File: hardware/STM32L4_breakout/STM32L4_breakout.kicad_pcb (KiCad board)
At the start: 2 copper layers, 64 parts, among them J1 12V IN, J10 GPIO, J11 SPI1, J12 USART1, J13 USART3, J14 UART4, J15 3.3V, J16 5V, J17 12V, J2 SWD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

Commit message: breakout board PCB layout WIP
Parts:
- J2: footprint Connector_PinHeader_2.54mm:PinHeader_2x05_P2.54mm_Vertical -> Connector_PinHeader_2.54mm:PinHeader_1x06_P2.54mm_Vertical
- moved J2 109.7 mm to (145.5, 78.8), turned to 180 degrees
- moved C12 51.1 mm to (157.5, 69.5), turned to 90 degrees
- moved C11 51.0 mm to (157.5, 67.0), turned to -90 degrees
- moved X1 40.6 mm to (155.5, 68.2), turned to -90 degrees
- moved L1 39.5 mm to (158.2, 79.0)
- moved C21 34.7 mm to (159.5, 74.0), turned to 90 degrees
- moved C13 32.4 mm to (164.5, 79.2), turned to 180 degrees
- moved C20 31.9 mm to (158.5, 77.0), turned to 180 degrees
- moved C14 31.5 mm to (171.0, 79.2), turned to 180 degrees
- moved R18 29.3 mm to (159.2, 69.0)
- moved R16 27.4 mm to (159.2, 67.5)
- moved C16 22.8 mm to (175.8, 67.8), turned to -90 degrees
- moved C15 19.3 mm to (158.8, 71.5), turned to 180 degrees
- moved C18 6.47 mm to (164.2, 61.0)
- moved C19 5.41 mm to (177.8, 67.8), turned to 90 degrees
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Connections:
- J2 pad 3: GND -> SWCLK
- J2 pad 4: SWCLK -> SWO
- J2 pad 5: GND -> STM_NRST
- J2 pad 6: SWO -> GND

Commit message: breakout board PCB layout WIP
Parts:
- C11, C12: footprint Capacitor_SMD:C_0603_1608Metric -> Capacitor_SMD:C_0402_1005Metric
- R16, R18: footprint Resistor_SMD:R_0603_1608Metric -> Resistor_SMD:R_0402_1005Metric
- moved J1 96.3 mm to (129.9, 67.5), turned to -90 degrees
- moved J12 94.1 mm to (178.0, 47.5), turned to 90 degrees
- moved J9 89.6 mm to (149.5, 70.7)
- moved C2 89.5 mm to (161.2, 47.5), turned to -90 degrees
- moved C4 86.8 mm to (163.5, 47.2), turned to -90 degrees
- moved C6 83.9 mm to (168.8, 50.2)
- moved U2 81.5 mm to (166.8, 47.5)
- moved C3 80.7 mm to (142.8, 60.5), turned to 90 degrees
- moved C7 80.0 mm to (170.2, 47.5), turned to -90 degrees
- moved J8 77.4 mm to (169.2, 84.8), turned to 90 degrees
- moved C9 75.8 mm to (172.5, 47.2), turned to -90 degrees
- moved C1 74.6 mm to (128.8, 60.5), turned to 90 degrees
- moved J11 73.7 mm to (166.5, 89.5), turned to 90 degrees
- moved U1 72.9 mm to (135.8, 59.0), turned to 0 degrees
- moved C5 68.9 mm to (145.5, 60.5), turned to 90 degrees
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
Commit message: breakout board PCB layout WIP
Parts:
- C11, C12: footprint Capacitor_SMD:C_0402_1005Metric -> Capacitor_SMD:C_0603_1608Metric
- R16, R18: footprint Resistor_SMD:R_0402_1005Metric -> Resistor_SMD:R_0603_1608Metric
- moved J14 111.5 mm to (149.5, 78.0)
- moved J13 96.7 mm to (150.0, 93.8), turned to 90 degrees
- moved J10 24.1 mm to (197.8, 62.8)
- moved J8 12.6 mm to (178.0, 93.8)
- moved J7 4.75 mm to (187.5, 62.5)
- moved J11 4.52 mm to (165.0, 93.8)
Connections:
- J10 pad 2: TFT_CS -> RELAY2_CTRL
- J10 pad 3: CARDCS_5V -> TFT_DC
- J10 pad 4: D7 -> RT_CS
- J10 pad 5: TFT_DC -> RELAY1_CTRL
- J10 pad 7: RELAY1_CTRL -> D7
- J10 pad 8: RT_CS -> CARDCS_5V
- J10 pad 9: RELAY2_CTRL -> TFT_CS

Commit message: breakout board layout WIP
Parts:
- moved R15 52.1 mm to (123.3, 110.7), turned to -90 degrees
- moved R14 34.4 mm to (128.1, 146.7), turned to 90 degrees
- moved J3 31.4 mm to (128.1, 139.1), turned to 90 degrees
- moved R12 29.8 mm to (166.2, 145.5), turned to 90 degrees
- moved R11 26.9 mm to (163.7, 145.5), turned to 90 degrees
- moved J6 25.6 mm to (168.3, 114.8), turned to -90 degrees
- moved R10 24.0 mm to (161.1, 145.5), turned to 90 degrees
- moved J5 22.6 mm to (141.1, 116.3), turned to -90 degrees
- moved R9 21.4 mm to (158.6, 145.5), turned to 90 degrees
- moved R13 19.3 mm to (145.9, 149.3), turned to -90 degrees
- moved R8 19.2 mm to (156.0, 145.5), turned to 90 degrees
- moved R7 17.3 mm to (153.5, 145.5), turned to 90 degrees
- moved J4 6.19 mm to (153.5, 139.1), turned to 90 degrees
- moved R4 1.31 mm to (105.5, 127.0)
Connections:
- net Net-(J5-Pad8) renamed /ARD_3V3A
- net Net-(R1-Pad2) renamed /I2C_PULL_3V3

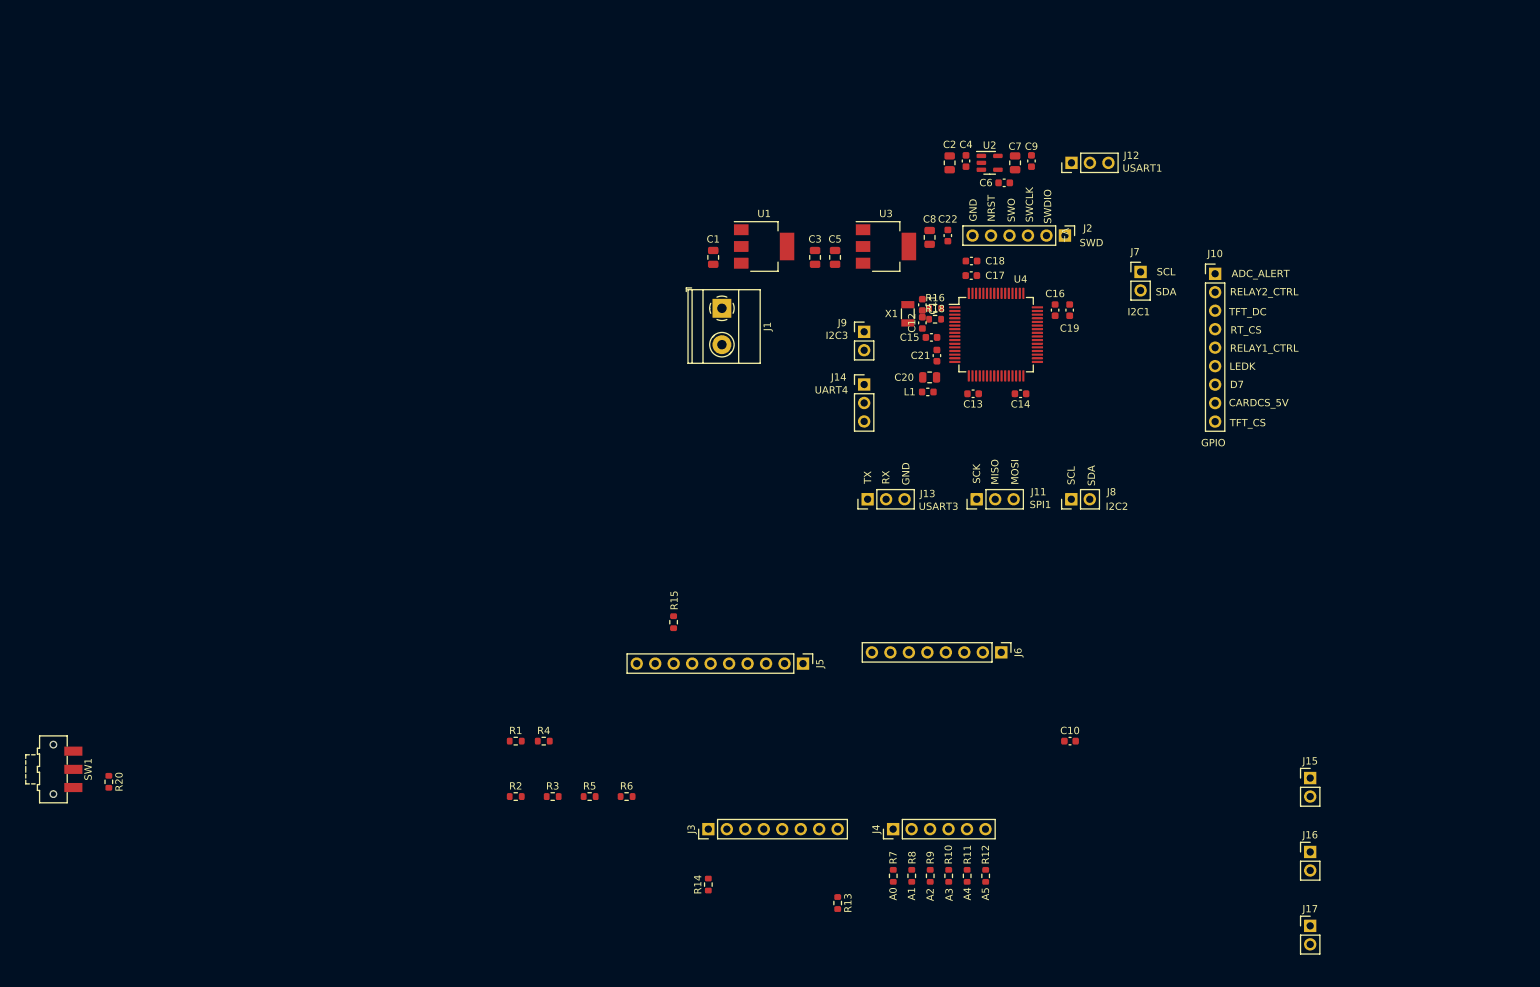
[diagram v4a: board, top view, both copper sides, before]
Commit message: breakout board pcb layout WIP
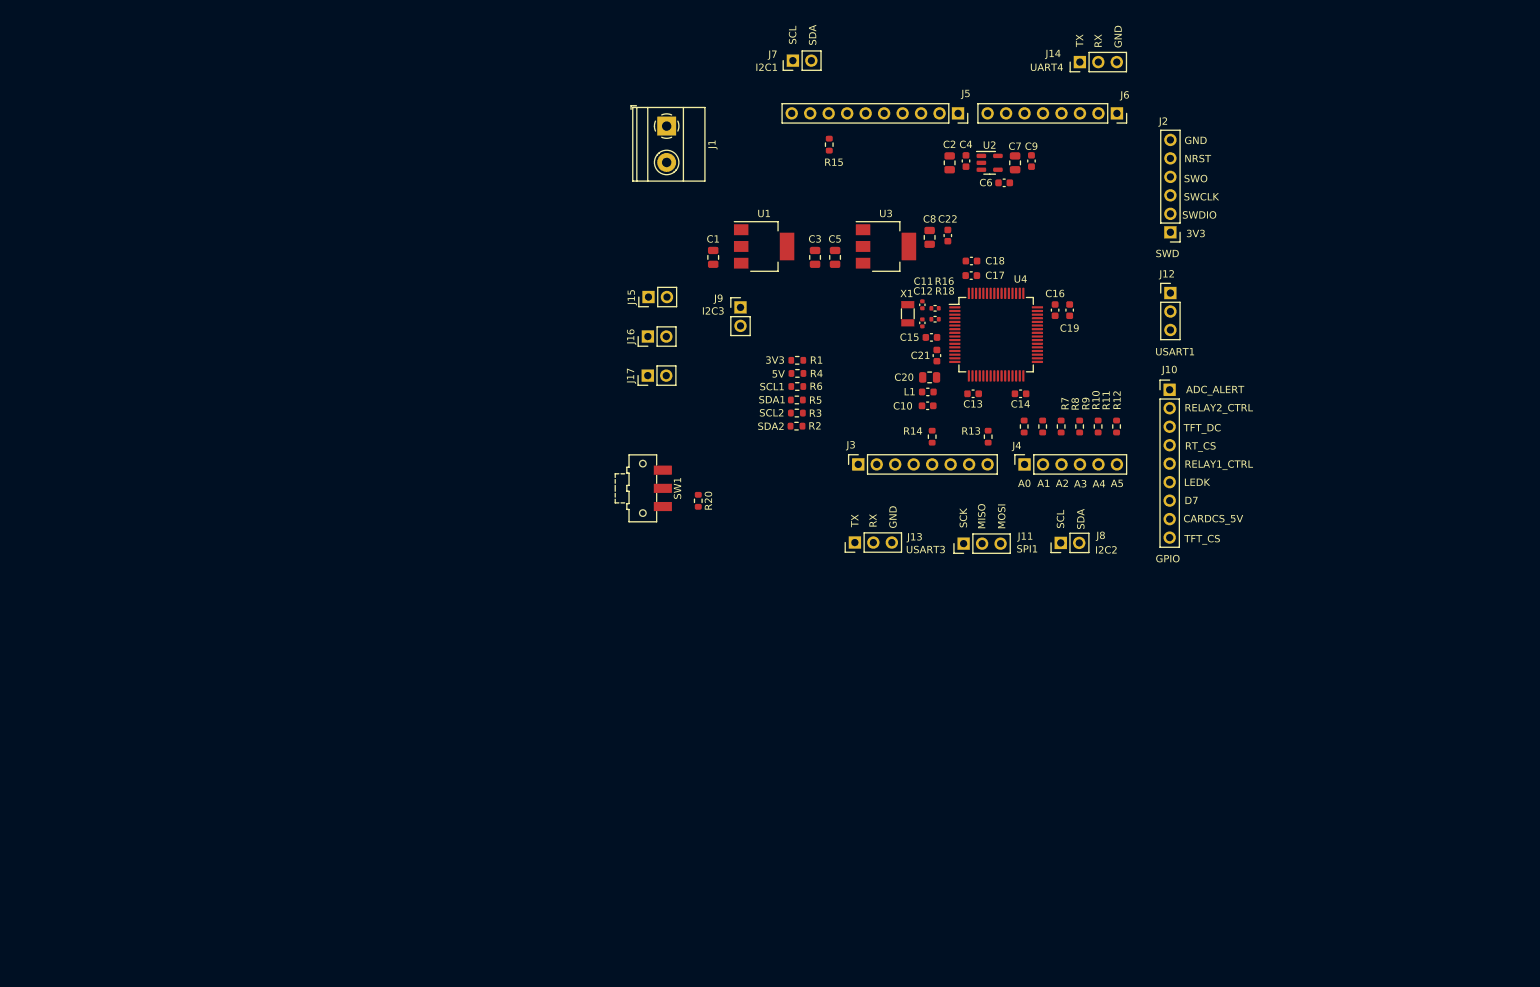
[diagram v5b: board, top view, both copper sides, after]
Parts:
- C11, C12: footprint Capacitor_SMD:C_0603_1608Metric -> Capacitor_SMD:C_0402_1005Metric
- J3, J6: footprint Connector_PinHeader_2.54mm:PinHeader_1x08_P2.54mm_Vertical -> Connector_PinSocket_2.54mm:PinSocket_1x08_P2.54mm_Vertical
- J4: footprint Connector_PinHeader_2.54mm:PinHeader_1x06_P2.54mm_Vertical -> Connector_PinSocket_2.54mm:PinSocket_1x06_P2.54mm_Vertical
- J5: footprint Connector_PinHeader_2.54mm:PinHeader_1x10_P2.54mm_Vertical -> Connector_PinSocket_2.54mm:PinSocket_1x10_P2.54mm_Vertical
- R16, R18: footprint Resistor_SMD:R_0603_1608Metric -> Resistor_SMD:R_0402_1005Metric
- moved J17 118.4 mm to (119.8, 76.8), turned to 90 degrees
- moved J16 115.4 mm to (119.8, 71.4), turned to 90 degrees
- moved J15 112.5 mm to (119.8, 66.0), turned to 90 degrees
- moved R20 89.8 mm to (126.7, 94.0)
- moved SW1 89.8 mm to (119.1, 92.2)
- moved J5 78.6 mm to (162.4, 40.7)
- moved J6 75.8 mm to (184.2, 40.7)
- moved R15 69.0 mm to (144.7, 45.0)
- moved R14 68.8 mm to (158.8, 85.2), turned to -90 degrees
- moved R13 67.4 mm to (166.6, 85.2), turned to 90 degrees
- moved R1 65.1 mm to (140.3, 74.7)
- moved R10 64.3 mm to (179.1, 83.8)
- moved R11 64.3 mm to (181.7, 83.8)
- moved R12 64.3 mm to (184.2, 83.8)
- moved R7 64.3 mm to (171.5, 83.8)
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
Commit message: breakout board pcb layout WIP - ready for outline
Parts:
- removed R4: 0 - DNI, Resistor_SMD:R_0603_1608Metric
- added H1: MountingHole_Pad, MountingHole:MountingHole_3.2mm_M3_DIN965_Pad_TopOnly, F.Cu at (115.2, 31.9)
- added H2: MountingHole_Pad, MountingHole:MountingHole_3.2mm_M3_DIN965_Pad_TopOnly, F.Cu at (204.1, 31.9)
- added H3: MountingHole_Pad, MountingHole:MountingHole_3.2mm_M3_DIN965_Pad_TopOnly, F.Cu at (204.1, 101.8)
- added H4: MountingHole_Pad, MountingHole:MountingHole_3.2mm_M3_DIN965_Pad_TopOnly, F.Cu at (115.2, 101.8)
- moved J17 15.3 mm to (118.4, 61.5)
- moved R20 11.9 mm to (126.3, 82.1)
- moved SW1 11.9 mm to (118.7, 80.3)
- moved J16 5.34 mm to (118.3, 66.2)
- moved J15 5.34 mm to (118.3, 71.0)
- moved J14 5.15 mm to (184.3, 33.5), turned to -90 degrees
- moved C15 3.68 mm to (155.1, 71.8)
- moved J9 2.49 mm to (134.8, 68.5)
- moved R1 2.36 mm to (140.5, 77.0)
- moved J1 2.00 mm to (120.3, 42.5)
- moved C21 0.70 mm to (159.6, 73.3)
- moved C11 0.50 mm to (157.4, 67.5)
- moved C12 0.50 mm to (157.4, 70.0)
- moved R16 0.50 mm to (159.2, 68.0)
- moved R18 0.50 mm to (159.2, 69.5)
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
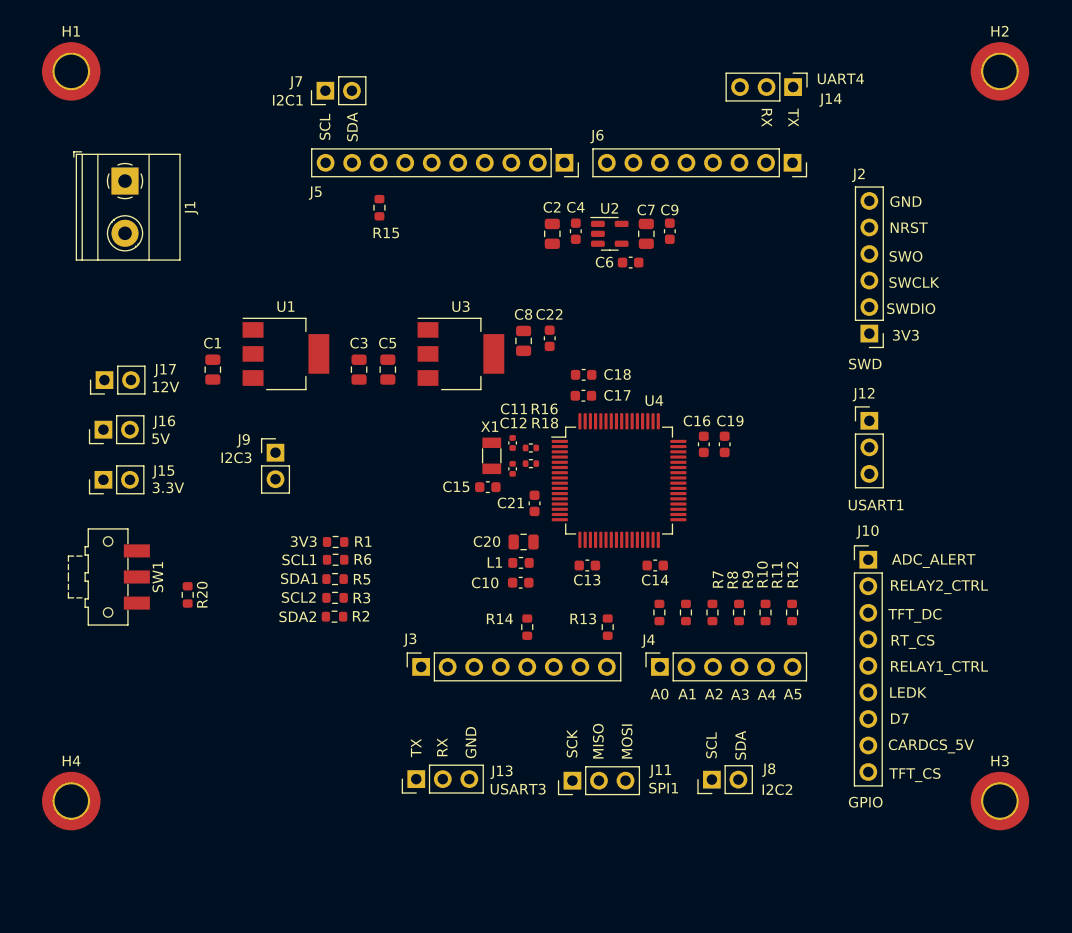
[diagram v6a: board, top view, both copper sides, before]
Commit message: created PCB outline
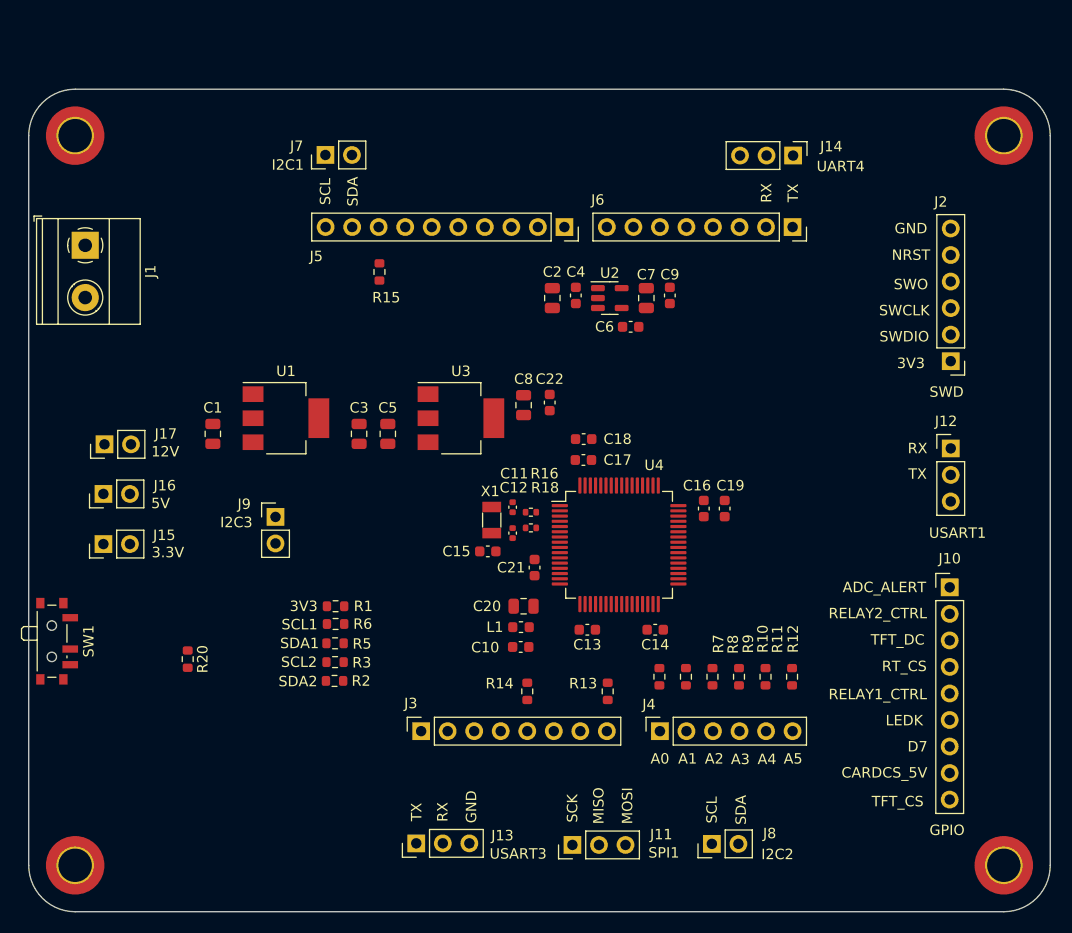
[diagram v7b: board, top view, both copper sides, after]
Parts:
- SW1: footprint Button_Switch_SMD:SW_SPDT_CK-JS102011SAQN -> Button_Switch_SMD:SW_SPDT_PCM12
- moved J10 8.23 mm to (199.3, 81.3)
- moved J12 8.23 mm to (199.4, 68.0)
- moved J2 8.23 mm to (199.4, 59.7)
- moved SW1 7.96 mm to (113.7, 86.5)
- moved J1 7.23 mm to (116.5, 48.6)
- moved J14 6.55 mm to (184.3, 40.0)
- moved H3 6.16 mm to (204.5, 108.0)
- moved H4 6.16 mm to (115.6, 108.0)
- moved H2 6.16 mm to (204.5, 38.1)
- moved H1 6.16 mm to (115.6, 38.1)
- moved C1 6.15 mm to (128.8, 66.7)
- moved C11 6.15 mm to (157.4, 73.7)
- moved C12 6.15 mm to (157.4, 76.2)
- moved C13 6.15 mm to (164.6, 85.4)
- moved C14 6.15 mm to (171.1, 85.4)
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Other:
- board outline added: 97.8 x 78.7 mm

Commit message: minor tweaks
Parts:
- moved J9 31.3 mm to (135.9, 105.9), turned to 90 degrees
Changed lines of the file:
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@@
   )
   (footprint "Connector_PinHeader_2.54mm:PinHeader_1x02_P2.54mm_Vertical" (layer "F.Cu")
-    (at 134.75 74.6)
+    (at 135.885 105.918 90)
     (descr "Through hole straight pin header, 1x02, 2.54mm pitch, single row")
     (tags "Through hole pin header THT 1x02 2.54mm single row")
@@
     (property "Sheetname" "")
     (attr through_hole)
-    (fp_text reference "J9" (at -3 -1.225) (layer "F.SilkS")
+    (fp_text reference "J9" (at 1.016 5.593 180) (layer "F.SilkS")
       (effects (font (size 1 1) (thickness 0.15)))
     )
-    (fp_text value "I2C3" (at -3.75 0.525) (layer "F.SilkS")
+    (fp_text value "I2C3" (at -0.762 6.355 180) (layer "F.SilkS")
       (effects (font (size 1 1) (thickness 0.15)))
     )
-    (fp_text user "${REFERENCE}" (at 0 1.27 90) (layer "F.Fab")
+    (fp_text user "SCL" (at 3.556 0.005 90 unlocked) (layer "F.SilkS")
+      (effects (font (size 1 1) (thickness 0.15)))
+    )
+    (fp_text user "SDA" (at 3.556 2.545 90 unlocked) (layer "F.SilkS")
+      (effects (font (size 1 1) (thickness 0.15)))
+    )
+    (fp_text user "${REFERENCE}" (at 0 1.27) (layer "F.Fab")
       (effects (font (size 1 1) (thickness 0.15)))
     )
@@
     (fp_line (start -0.635 -1.27) (end 1.27 -1.27) (layer "F.Fab") (width 0.1))
     (fp_line (start -1.27 3.81) (end -1.27 -0.635) (layer "F.Fab") (width 0.1))
-    (pad "1" thru_hole rect (at 0 0) (size 1.7 1.7) (drill 1) (layers *.Cu *.Mask)
+    (pad "1" thru_hole rect (at 0 0 90) (size 1.7 1.7) (drill 1) (layers *.Cu *.Mask)
       (net 41 "I2C3_SCL") (pinfunction "Pin_1") (pintype "passive"))
-    (pad "2" thru_hole oval (at 0 2.54) (size 1.7 1.7) (drill 1) (layers *.Cu *.Mask)
+    (pad "2" thru_hole oval (at 0 2.54 90) (size 1.7 1.7) (drill 1) (layers *.Cu *.Mask)
       (net 42 "I2C3_SDA") (pinfunction "Pin_2") (pintype "passive"))
     (model "${KICAD6_3DMODEL_DIR}/Connector_PinHeader_2.54mm.3dshapes/PinHeader_1x02_P2.54mm_Vertical.wrl"
